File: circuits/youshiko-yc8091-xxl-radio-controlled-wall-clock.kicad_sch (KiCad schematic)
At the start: 13 parts, among them Q1 PMOS, U1 ESP32-S3-WROOM-1

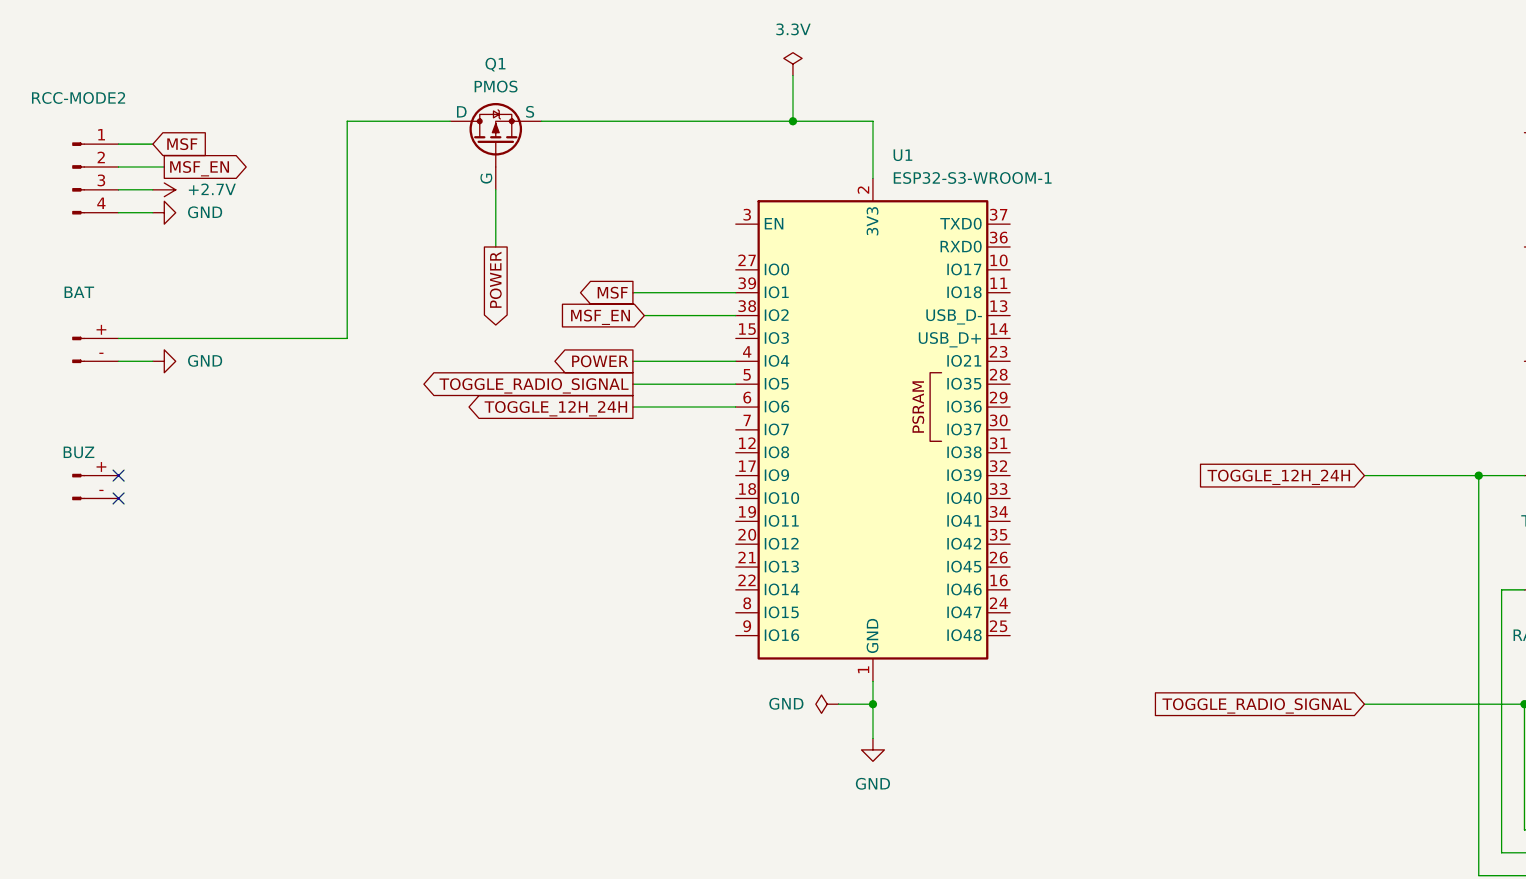
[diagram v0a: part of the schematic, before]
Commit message: Indicate active low on schematic
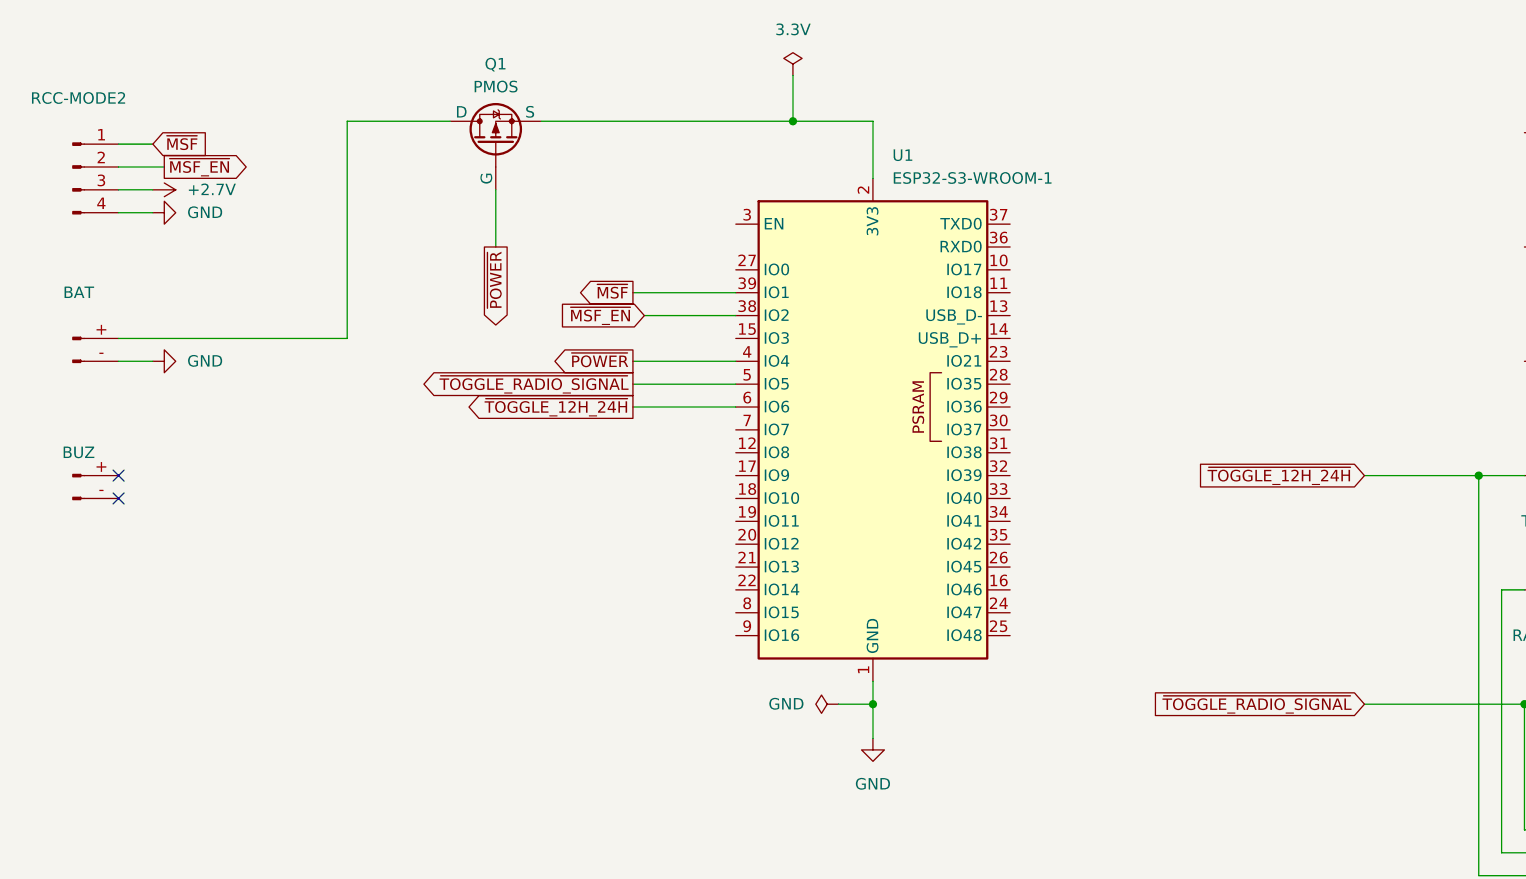
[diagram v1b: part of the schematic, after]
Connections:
- net MSF renamed ~{MSF}
- net MSF_EN renamed ~{MSF_EN}
- net POWER renamed ~{POWER}
- net TOGGLE_12H_24H renamed ~{TOGGLE_12H_24H}
- net TOGGLE_RADIO_SIGNAL renamed ~{TOGGLE_RADIO_SIGNAL}
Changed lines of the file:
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@@
 		)
 	)
-	(global_label "TOGGLE_RADIO_SIGNAL"
+	(global_label "~{TOGGLE_RADIO_SIGNAL}"
 		(shape input)
 		(at 181.61 96.52 180)
@@
 		)
 		(property "Intersheetrefs" "${INTERSHEET_REFS}"
-			(at 157.579 96.52 0)
-			(effects
-				(font
-					(size 1.27 1.27)
-				)
-				(justify right)
-				(hide yes)
-			)
-		)
-	)
-	(global_label "TOGGLE_RADIO_SIGNAL"
+			(at 156.309 96.52 0)
+			(effects
+				(font
+					(size 1.27 1.27)
+				)
+				(justify right)
+				(hide yes)
+			)
+		)
+	)
+	(global_label "~{TOGGLE_RADIO_SIGNAL}"
 		(shape output)
 		(at 100.33 60.96 180)
@@
 		)
 		(property "Intersheetrefs" "${INTERSHEET_REFS}"
-			(at 76.299 60.96 0)
-			(effects
-				(font
-					(size 1.27 1.27)
-				)
-				(justify right)
-				(hide yes)
-			)
-		)
-	)
-	(global_label "TOGGLE_12H_24H"
+			(at 75.029 60.96 0)
+			(effects
+				(font
+					(size 1.27 1.27)
+				)
+				(justify right)
+				(hide yes)
+			)
+		)
+	)
+	(global_label "~{TOGGLE_12H_24H}"
 		(shape input)
 		(at 181.61 71.12 180)
@@
 		)
 		(property "Intersheetrefs" "${INTERSHEET_REFS}"
-			(at 162.1754 71.12 0)
-			(effects
-				(font
-					(size 1.27 1.27)
-				)
-				(justify right)
-				(hide yes)
-			)
-		)
-	)
-	(global_label "MSF"
+			(at 160.9054 71.12 0)
+			(effects
+				(font
+					(size 1.27 1.27)
+				)
+				(justify right)
+				(hide yes)
+			)
+		)
+	)
+	(global_label "~{MSF}"
 		(shape output)
 		(at 100.33 50.8 180)
@@
 		)
 		(property "Intersheetrefs" "${INTERSHEET_REFS}"
-			(at 93.5953 50.8 0)
-			(effects
-				(font
-					(size 1.27 1.27)
-				)
-				(justify right)
-				(hide yes)
-			)
-		)
-	)
-	(global_label "MSF"
+			(at 92.3253 50.8 0)
+			(effects
+				(font
+					(size 1.27 1.27)
+				)
+				(justify right)
+				(hide yes)
+			)
+		)
+	)
+	(global_label "~{MSF}"
 		(shape input)
 		(at 46.99 34.29 0)
@@
 		)
 		(property "Intersheetrefs" "${INTERSHEET_REFS}"
-			(at 53.7247 34.29 0)
+			(at 54.9947 34.29 0)
 			(effects
 				(font
@@
 		)
 	)
-	(global_label "MSF_EN"
+	(global_label "~{MSF_EN}"
 		(shape output)
 		(at 48.26 36.83 0)
@@
 		)
 		(property "Intersheetrefs" "${INTERSHEET_REFS}"
-			(at 58.4418 36.83 0)
+			(at 59.7118 36.83 0)
 			(effects
 				(font
@@
 		)
 	)
-	(global_label "POWER"
+	(global_label "~{POWER}"
 		(shape output)
 		(at 100.33 58.42 180)
@@
 		)
 		(property "Intersheetrefs" "${INTERSHEET_REFS}"
-			(at 90.8739 58.42 0)
-			(effects
-				(font
-					(size 1.27 1.27)
-				)
-				(justify right)
-				(hide yes)
-			)
-		)
-	)
-	(global_label "POWER"
+			(at 89.6039 58.42 0)
+			(effects
+				(font
+					(size 1.27 1.27)
+				)
+				(justify right)
+				(hide yes)
+			)
+		)
+	)
+	(global_label "~{POWER}"
 		(shape output)
 		(at 85.09 45.72 270)
@@
 		)
 	)
-	(global_label "TOGGLE_12H_24H"
+	(global_label "~{TOGGLE_12H_24H}"
 		(shape output)
 		(at 100.33 63.5 180)
@@
 		)
 		(property "Intersheetrefs" "${INTERSHEET_REFS}"
-			(at 80.8954 63.5 0)
-			(effects
-				(font
-					(size 1.27 1.27)
-				)
-				(justify right)
-				(hide yes)
-			)
-		)
-	)
-	(global_label "MSF_EN"
+			(at 79.6254 63.5 0)
+			(effects
+				(font
+					(size 1.27 1.27)
+				)
+				(justify right)
+				(hide yes)
+			)
+		)
+	)
+	(global_label "~{MSF_EN}"
 		(shape input)
 		(at 101.6 53.34 180)
@@
 		)
 		(property "Intersheetrefs" "${INTERSHEET_REFS}"
-			(at 91.4182 53.34 0)
-			(effects
-				(font
+			(at 90.1482 53.34 0)
+			(effects
+				(font

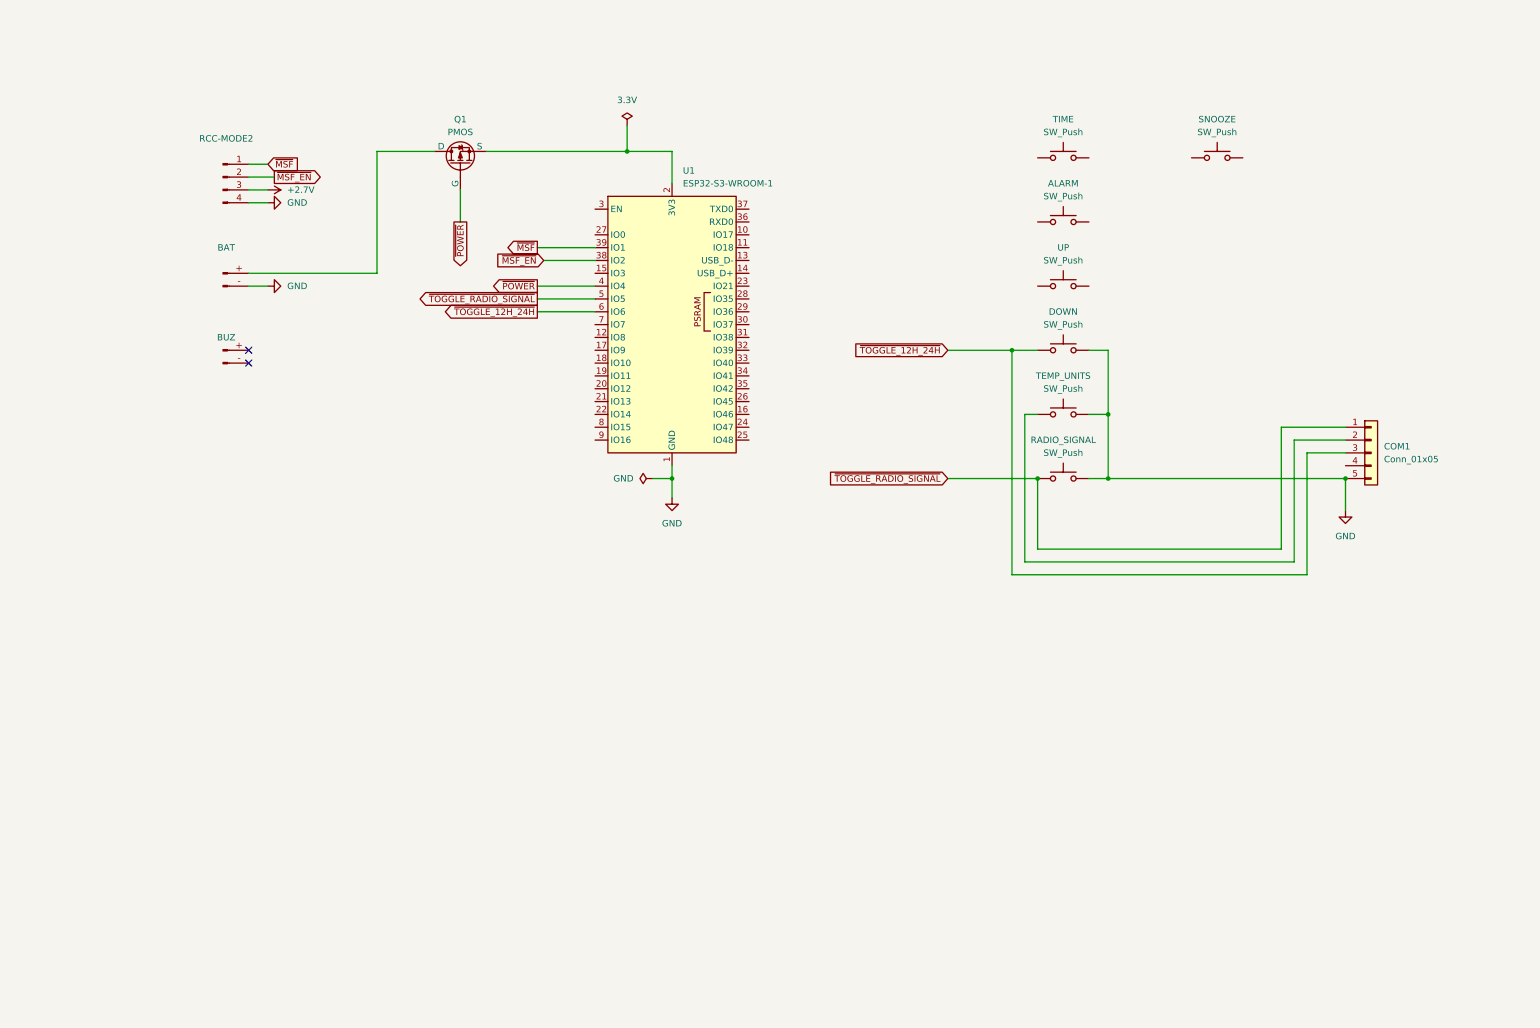
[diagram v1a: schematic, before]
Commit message: Layout schematic to match the physical layout and render schematic to SVG
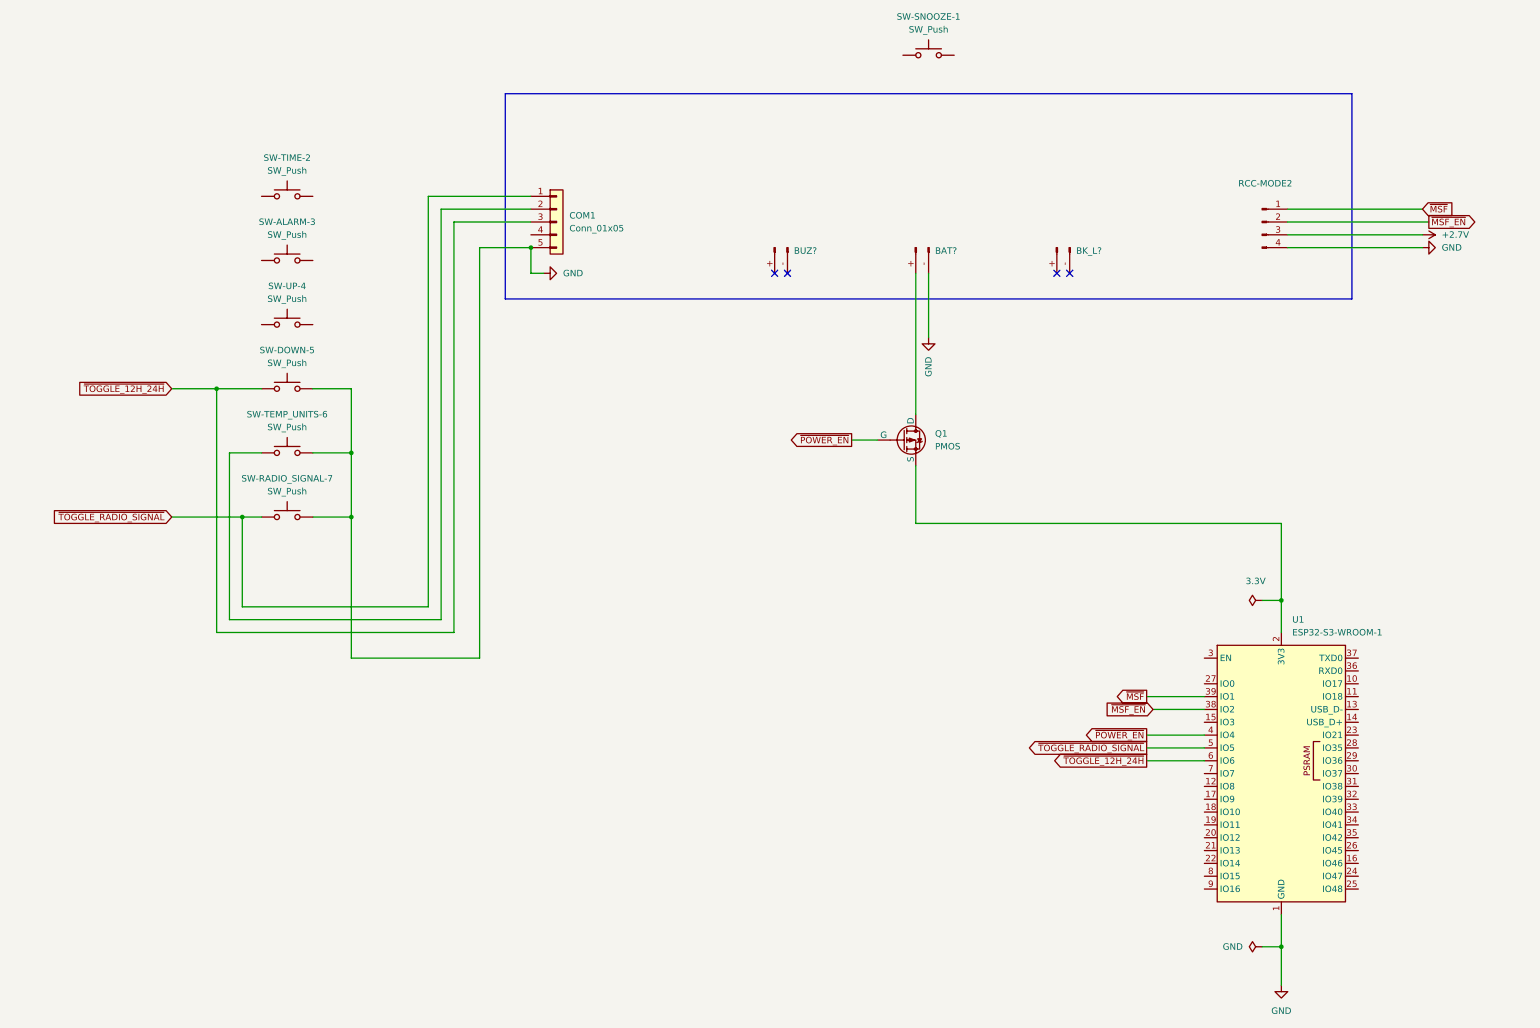
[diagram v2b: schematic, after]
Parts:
- added BK_L?: Conn_01x02_Pin, symbol Connector:Conn_01x02_Pin
- renumbered BAT to BAT?, BUZ to BUZ?, ALARM to SW-ALARM-3, DOWN to SW-DOWN-5, RADIO_SIGNAL to SW-RADIO_SIGNAL-7, SNOOZE to SW-SNOOZE-1, TEMP_UNITS to SW-TEMP_UNITS-6, TIME to SW-TIME-2, UP to SW-UP-4
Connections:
- net ~{POWER} renamed ~{POWER_EN}
- no-connect marks 2 -> 4
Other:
- moved on the sheet: BAT?, BUZ?, COM1, Q1, RCC-MODE2, SW-ALARM-3, SW-DOWN-5, SW-RADIO_SIGNAL-7, SW-SNOOZE-1, SW-TEMP_UNITS-6, SW-TIME-2, SW-UP-4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

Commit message: Make the schematic clearer on where to connect and that the 2.7V power is unused
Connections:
- net +2.7V: no longer names the net of RCC-MODE2.3 (Pin_3)
- no-connect marks 4 -> 5
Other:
- note added: "+2.7V (not used)"
- moved on the sheet: SW-ALARM-3, SW-DOWN-5, SW-RADIO_SIGNAL-7, SW-TEMP_UNITS-6, SW-TIME-2, SW-UP-4
